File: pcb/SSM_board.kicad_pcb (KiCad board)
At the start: 4 copper layers, 100 x 100 mm, 184 parts, among them IC1 STPIC6C595TTR, IC2 STPIC6C595TTR, IC3 STPIC6C595TTR, IC4 STPIC6C595TTR, IC5 STPIC6C595TTR, IC6 STPIC6C595TTR, IC7 STPIC6C595TTR, IC8 STPIC6C595TTR, J1 DA15_Pins_MountingHoles, J2 DA15_Pins_MountingHoles, U101 GAQY212GS, U102 GAQY212GS, U103 GAQY212GS, U104 GAQY212GS, U105 GAQY212GS, U106 GAQY212GS, U107 GAQY212GS, U108 GAQY212GS, U201 GAQY212GS, U202 GAQY212GS, U203 GAQY212GS, U204 GAQY212GS, U205 GAQY212GS, U206 GAQY212GS, U207 GAQY212GS, U208 GAQY212GS, U301 GAQY212GS, U302 GAQY212GS, U303 GAQY212GS, U304 GAQY212GS, U305 GAQY212GS, U306 GAQY212GS, U307 GAQY212GS, U308 GAQY212GS, U401 GAQY212GS, U402 GAQY212GS, U403 GAQY212GS, U404 GAQY212GS, U405 GAQY212GS, U406 GAQY212GS, U407 GAQY212GS, U408 GAQY212GS, U501 GAQY212GS, U502 GAQY212GS, U503 GAQY212GS, U504 GAQY212GS, U505 GAQY212GS, U506 GAQY212GS, U507 GAQY212GS, U508 GAQY212GS, U601 GAQY212GS, U602 GAQY212GS, U603 GAQY212GS, U604 GAQY212GS, U605 GAQY212GS, U606 GAQY212GS, U607 GAQY212GS, U608 GAQY212GS, U609 GAQY212GS, U610 GAQY212GS, U611 GAQY212GS, U612 GAQY212GS, U701 GAQY212GS, U702 GAQY212GS, U703 GAQY212GS, U704 GAQY212GS, U705 GAQY212GS, U706 GAQY212GS, U707 GAQY212GS, U708 GAQY212GS, U709 GAQY212GS, U710 GAQY212GS, U711 GAQY212GS, U712 GAQY212GS

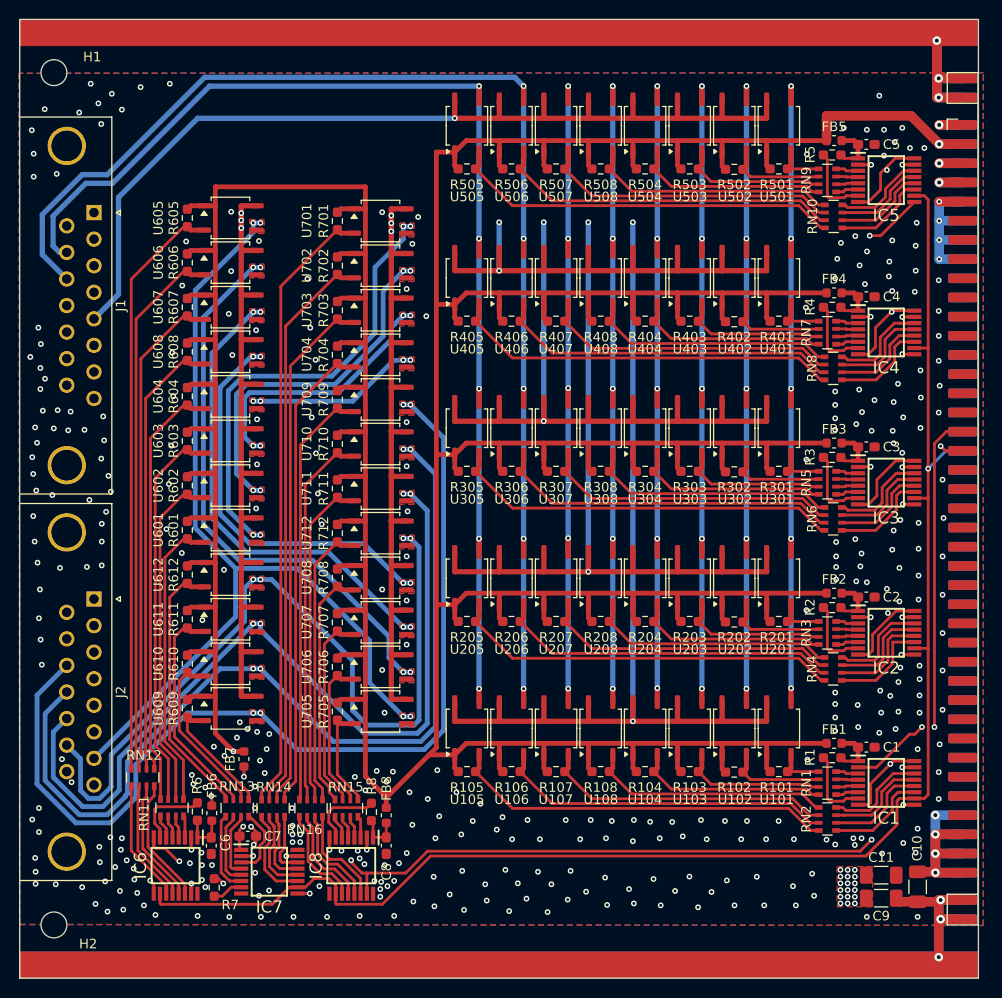
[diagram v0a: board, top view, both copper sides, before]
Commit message: Unify footprints, add via-in-pad DRC rule, regenerate outputs
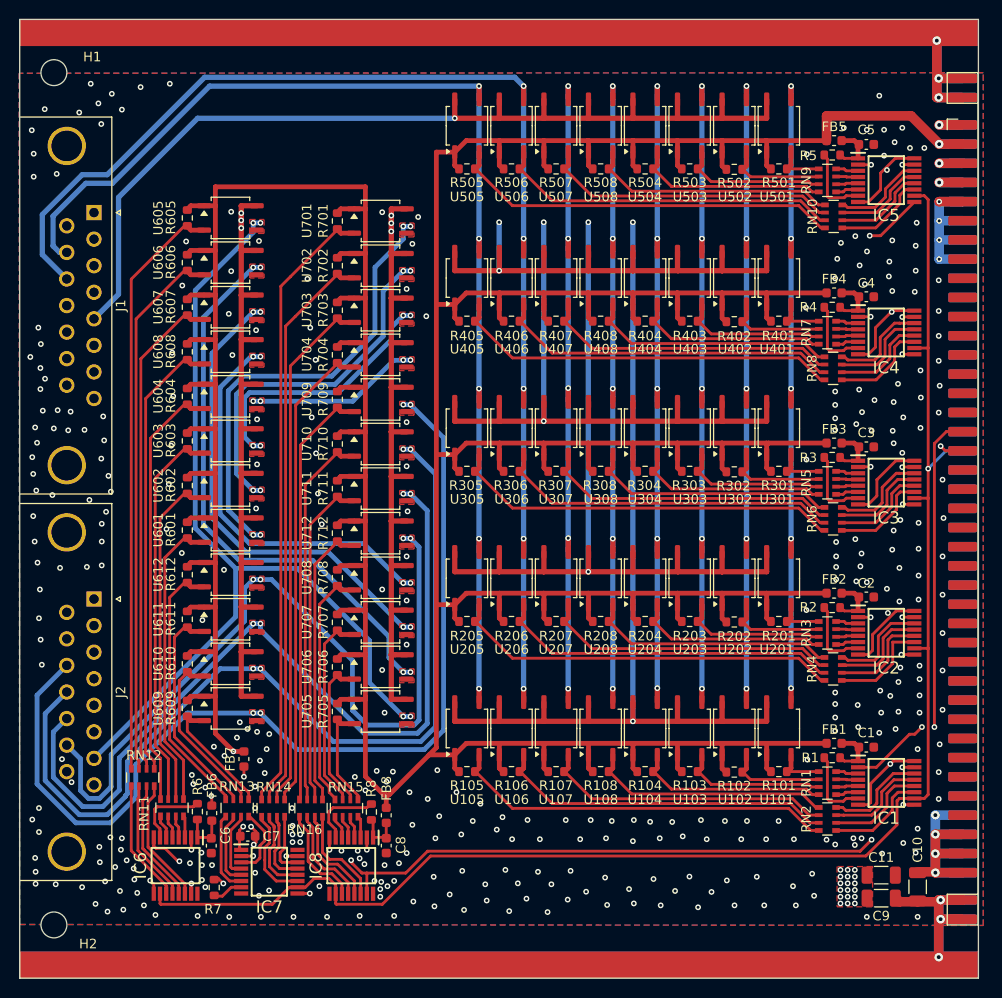
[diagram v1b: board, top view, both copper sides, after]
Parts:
- C1, C2, C3, C4, C5, C6, C7, C8: footprint Capacitor_SMD:C_0603_1608Metric_Pad1.08x0.95mm_HandSolder -> Capacitor_SMD:C_0603_1608Metric
- C10, C11, C9: footprint Capacitor_SMD:C_1206_3216Metric_Pad1.33x1.80mm_HandSolder -> Capacitor_SMD:C_1206_3216Metric
- R1, R101, R102, R103, R104, R105, R106, R107, R108, R2, R201, R202, R203, R204, R205, R206, R207, R208, R3, R301, R302, R303, R304, R305, R306, R307, R308, R4, R401, R402, R403, R404, R405, R406, R407, R408, R5, R501, R502, R503, R504, R505, R506, R507, R508, R6, R601, R602, R603, R604, R605, R606, R607, R608, R609, R610, R611, R612, R7, R701, R702, R703, R704, R705, R706, R707, R708, R709, R710, R711, R712, R8: footprint Resistor_SMD:R_0603_1608Metric_Pad0.98x0.95mm_HandSolder -> Resistor_SMD:R_0603_1608Metric
